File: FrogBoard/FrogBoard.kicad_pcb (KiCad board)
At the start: 2 copper layers, 59.3 x 50.6 mm, 66 parts, among them J1 Conn_01x10, J10 Conn_01x01, J11 Conn_01x01, J12 Conn_01x01, J13 Conn_01x01, J14 Conn_01x01, J15 Conn_01x01, J16 Conn_01x01, J17 Conn_01x01, J18 Conn_01x01, J19 Conn_01x01, J2 Conn_01x04, J20 Conn_01x01, J21 Conn_01x01, J22 Conn_01x01, J23 Conn_01x01, J24 Conn_01x01, J25 Conn_01x01, J26 USB_B_Micro, J29 Conn_01x01, J3 Conn_01x01, J30 Conn_01x01, J31 Conn_01x01, J32 Conn_01x01, J33 Conn_01x01, J34 Conn_01x01, J35 Conn_01x01, J36 Conn_01x01, J37 Conn_01x01, J4 Stickbox, J5 Conn_01x03_Socket, J6 Conn_01x02, J8 Conn_01x01, J9 Conn_01x01, U1 STM32L432KBUx, U2 USBLC6-2P6, U3 MCP1700T-3302E, U4 BL1555

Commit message: Fix silkscreens
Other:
- board text added: "A_SEL"
- board text added: "D+"
- board text added: "D-"
- board text added: "FrogBoard v1.0.0-rc2"
- board text added: "P2"
- board text added: "P3"
- board text added: "P4"
- board text added: "P5"
- board text added: "P6"
- board text added: "PA0"
- board text added: "PA1"
- board text added: "PA10"
- board text added: "PA13"
- board text added: "PA14"
- board text added: "PA15"
- board text added: "PA2"
- board text added: "PC14"
- board text added: "PC15"
- board text added: "SCL"
- board text added: "V+H"
- board text added: "X_O"
- board text added: "X_O_MUX"
- board text added: "Y_O"
- board text added: "Y_O_MUX"

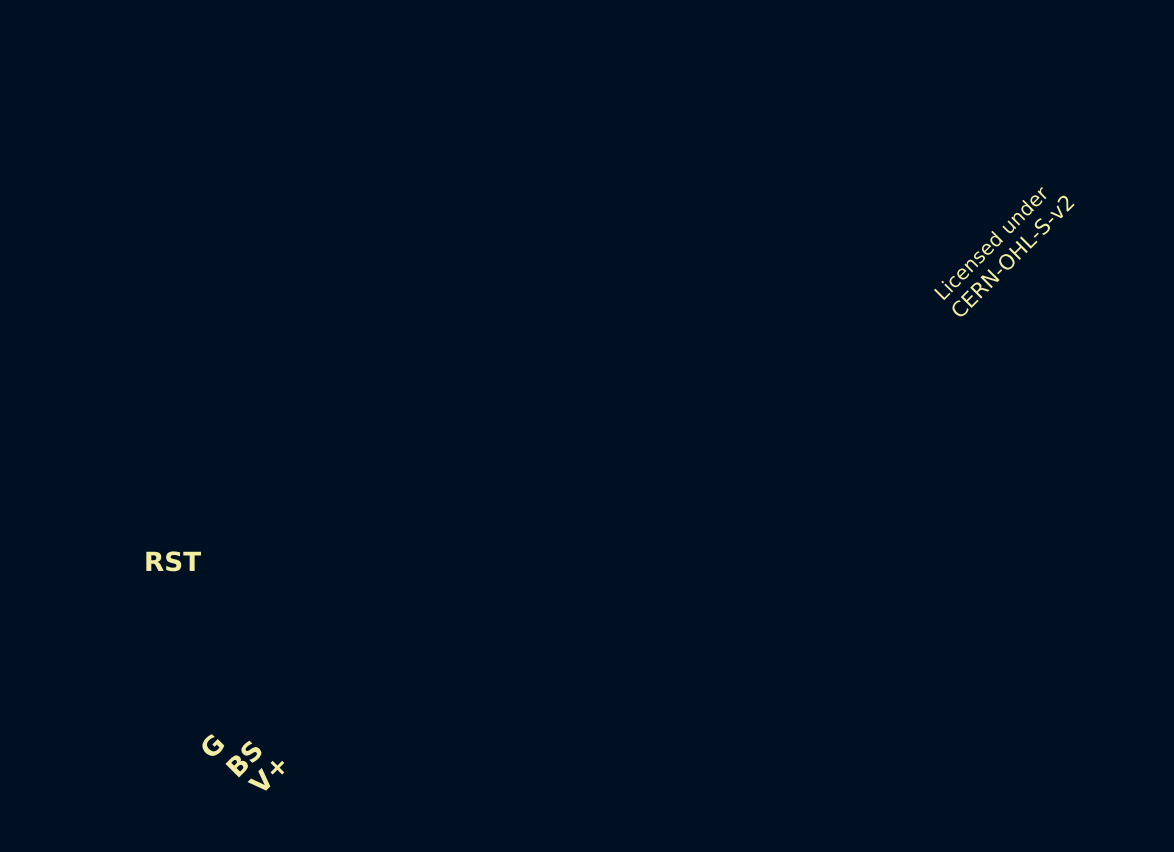
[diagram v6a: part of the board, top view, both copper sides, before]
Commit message: Add FrogBoard logo
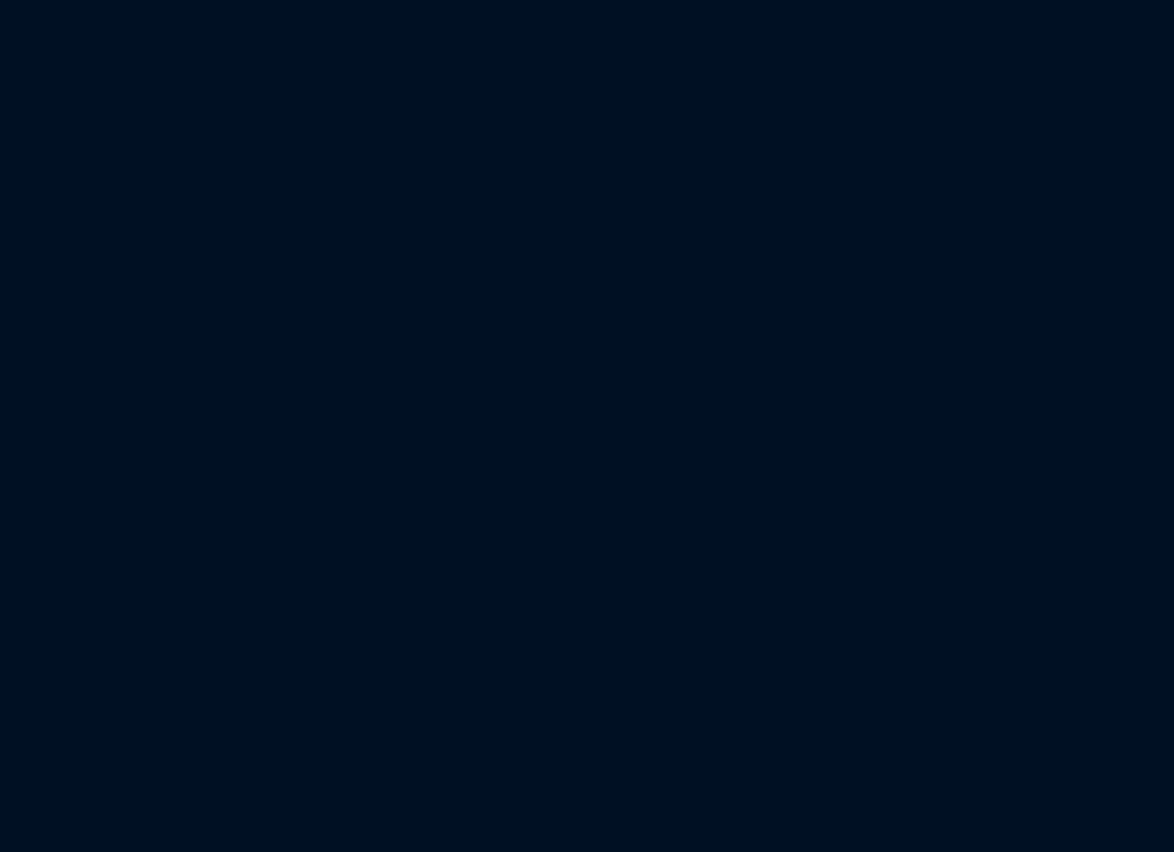
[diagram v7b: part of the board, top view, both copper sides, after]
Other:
- board text added: "v1.0.0-rc2"
- board text removed: "3.3v"
- board text removed: "BS"
- board text removed: "FrogBoard v1.0.0-rc1"
- board text removed: "FrogBoard v1.0.0-rc2"
- board text removed: "RST"
- board text removed: "SLC"
- board text removed: "X_v"
- board text removed: "Y_v"
- board text removed: "ZenithControlLabs"
